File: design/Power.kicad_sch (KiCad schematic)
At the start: 77 parts

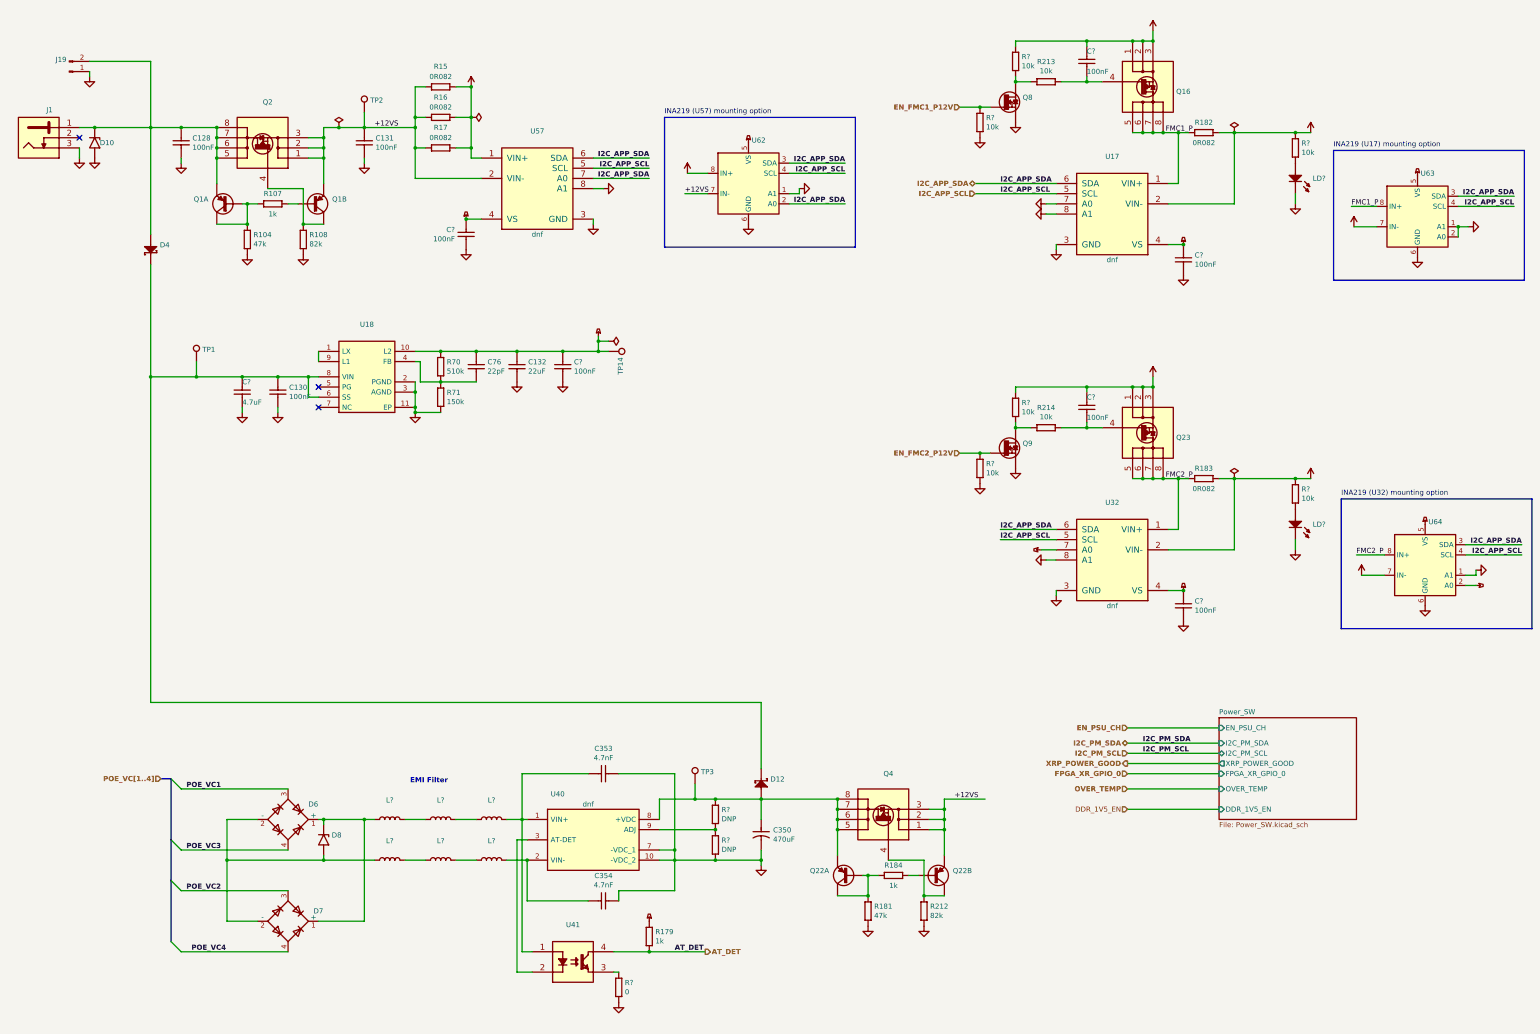
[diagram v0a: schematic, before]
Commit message: new power converter added
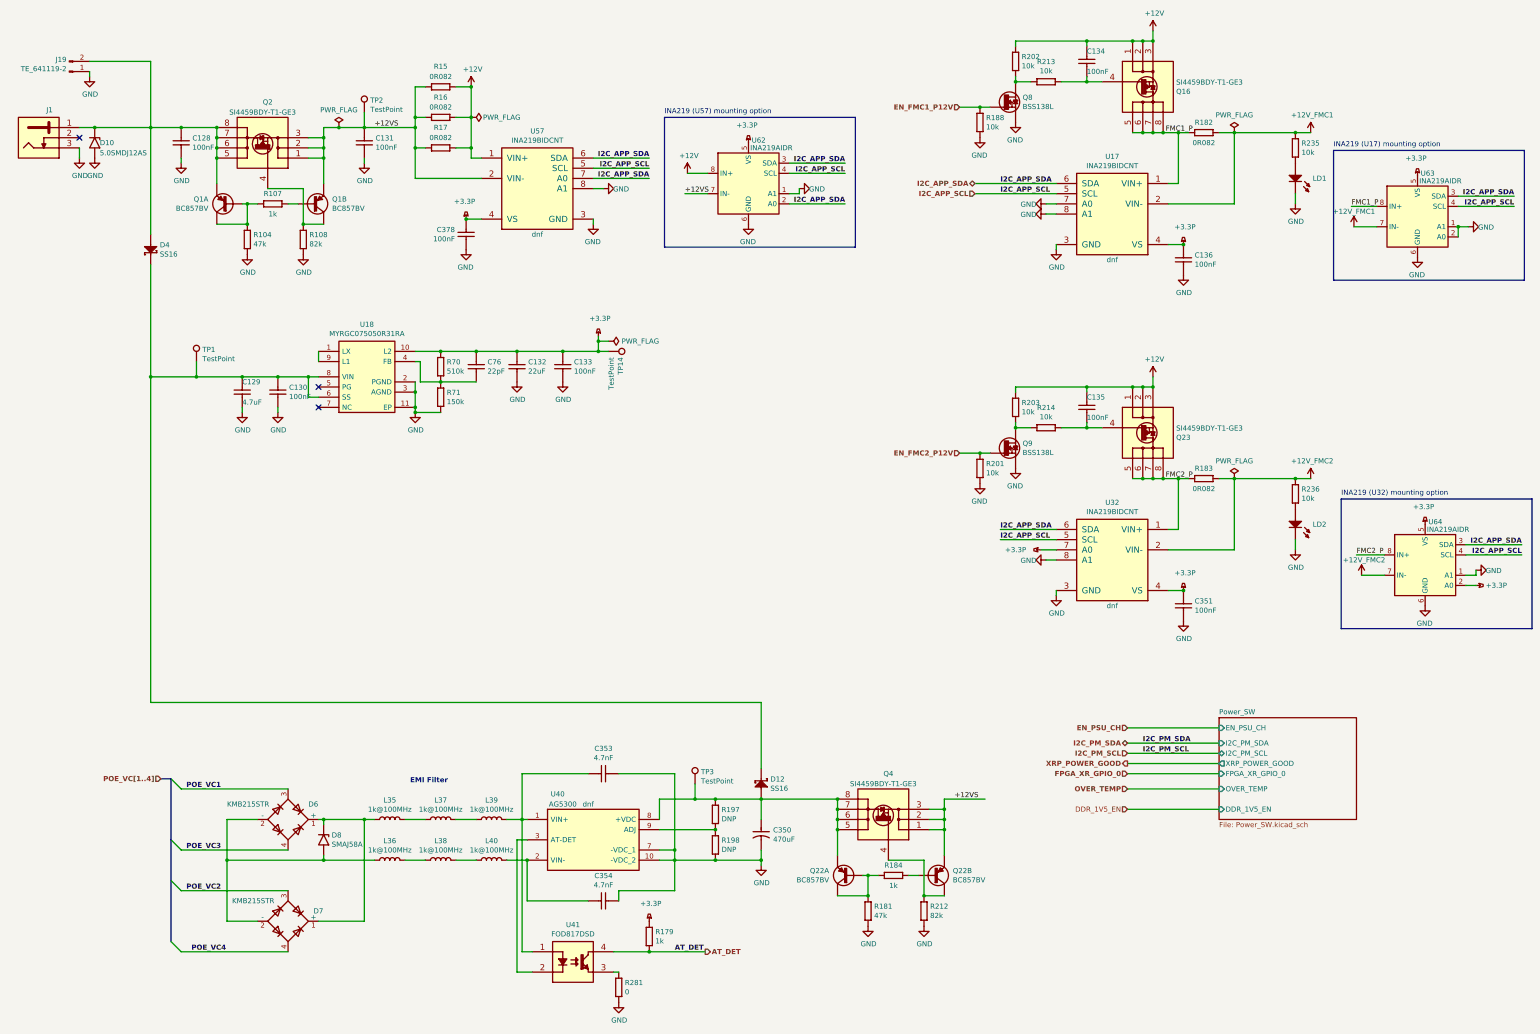
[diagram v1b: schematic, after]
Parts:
- C128, C130, C131: value (none) -> CC0402_100NF_25V_10%_X5R; footprint (none) -> Marble:CAPC1005X55N
- C129: renamed from C?; value (none) -> CC0603_4.7UF_25V_10%_X5R; footprint (none) -> Capacitors SMD:CAPC1608X90N
- C132: value (none) -> CC0603_22UF_6.3V_20%_X5R; footprint (none) -> CAPC1709X100N
- C133, C136, C351, C378: renamed from C?; value (none) -> CC0201_100NF_6.3V_10%_X5R; footprint (none) -> CAPC0603X33N
- C134, C135: renamed from C?; value (none) -> CC0402_100NF_25V_10%_X5R; footprint (none) -> Marble:CAPC1005X55N
- C350: value (none) -> CAE830-1020_470UF_16V_20%; footprint (none) -> CAPAE830X1020N
- C353, C354: value (none) -> CPER_4.7NF_400V_5%_500-250X720X650; footprint (none) -> CAPR500-250X720X650
- C76: value (none) -> CC0402_22PF_50V_5%_C0G; footprint (none) -> Capacitors SMD:CAPC1005X55N
- D10: value (none) -> 5.0SMDJ12AS; footprint (none) -> Diode_SMD:D_SMC
- D12, D4: value (none) -> SS16; footprint (none) -> DIOM5127X229N
- D6, D7: value (none) -> KMB215STR; footprint (none) -> ICs And Semiconductors SMD:SOIC254P665X290-4N
- D8: value (none) -> SMAJ58A; footprint (none) -> ICs And Semiconductors SMD:DIOM5226X262N
- J1: value (none) -> CLIFF_FC68148(DC-10A); footprint (none) -> Miscellaneous THD:CLIFF_FC68148(DC-10A)
- J19: value (none) -> TE_641119-2; footprint (none) -> Marble:641119-2
- L35, L36, L37, L38, L39, L40: renamed from L?; value (none) -> 1k@100MHz; footprint (none) -> Inductors SMD:INDC2012X145N
- LD1, LD2: renamed from LD?; value (none) -> LED_KINGBRIGHT_KPH-1608CGCK; footprint (none) -> ICs And Semiconductors SMD:LED_KINGBRIGHT_KPH-1608CGCK
- Q1, Q22: value (none) -> BC857BV; footprint (none) -> SOTFL50P160X60-6N
- Q16, Q2, Q23, Q4: value (none) -> SI4459BDY-T1-GE3; footprint (none) -> ICs And Semiconductors SMD:SOIC127P600X175-8N
- Q8, Q9: value (none) -> BSS138L; footprint (none) -> ICs And Semiconductors SMD:SOT95P240X110-3N
- R104, R181: value (none) -> R0402_47K_1%_0.0625W_100PPM; footprint (none) -> RESC1005X40N
- R107, R179, R184: value (none) -> R0402_1K_1%_0.0625W_100PPM; footprint (none) -> RESC1005X40N
- R108, R212: value (none) -> R0402_82K_1%_0.0625W_100PPM; footprint (none) -> RESC1005X40N
- R15, R16, R17, R182, R183: value (none) -> R1206_0R082_1%_0.5W_100PPM; footprint (none) -> RESC3216X80N
- R188, R201, R202, R203, R235, R236: renamed from R?; value (none) -> R0402_10K_1%_0.0625W_100PPM; footprint (none) -> RESC1005X40N
- R197, R198, R281: renamed from R?; value (none) -> R0402_0R_JUMPER; footprint (none) -> RESC1005X40N
- R213, R214: value (none) -> R0402_10K_1%_0.0625W_100PPM; footprint (none) -> RESC1005X40N
- R70: value (none) -> R0402_510K_1%_0.0625W_100PPM; footprint (none) -> Resistors SMD:RESC1005X40N
- R71: value (none) -> R0402_150K_1%_0.0625W_100PPM; footprint (none) -> Resistors SMD:RESC1005X40N
- TP1, TP14, TP2, TP3: value (none) -> TestPoint; footprint (none) -> TestPoint:TestPoint_THTPad_D1.5mm_Drill0.7mm
- U17, U32, U57: value (none) -> INA219BIDCNT; footprint (none) -> ICs And Semiconductors SMD:SOT65P280X145-8N
- U18: value (none) -> MYRGC075050R31RA; footprint (none) -> SamacSys_Parts:MYRGC075050
- U40: value (none) -> AG5300; footprint (none) -> AG5300:AG5300
- U41: value (none) -> FOD817DSD; footprint (none) -> FAIRCHILD_FOD817DSD
- U62, U63, U64: value (none) -> INA219AIDR; footprint (none) -> Package_SO:SOIC-8_3.9x4.9mm_P1.27mm

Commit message: fixed parts numners
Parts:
- C128, C130, C131, C134, C135: footprint Marble:CAPC1005X55N -> CAPC1005X55N; ALTIUM_VALUE (none) -> 100nF
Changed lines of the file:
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@@
       (effects (font (size 1.524 1.524)) (justify left) hide)
     )
-    (property "Footprint" "Marble:CAPC1005X55N" (id 2) (at 254.762 26.67 0)
+    (property "Footprint" "CAPC1005X55N" (id 2) (at 254.762 26.67 0)
       (effects (font (size 1.524 1.524)) (justify left) hide)
     )
@@
       (effects (font (size 1.524 1.524)) (justify left) hide)
     )
+    (property "ALTIUM_VALUE" "100nF" (id 40) (at 281.94 26.67 0)
+      (effects (font (size 1.27 1.27)) hide)
+    )
     (pin "1")
     (pin "2")
@@
       (effects (font (size 1.524 1.524)) (justify left) hide)
     )
-    (property "Footprint" "Marble:CAPC1005X55N" (id 2) (at 254.762 113.03 0)
+    (property "Footprint" "CAPC1005X55N" (id 2) (at 254.762 113.03 0)
       (effects (font (size 1.524 1.524)) (justify left) hide)
     )
@@
       (effects (font (size 1.524 1.524)) (justify left) hide)
     )
+    (property "ALTIUM_VALUE" "100nF" (id 40) (at 281.94 113.03 0)
+      (effects (font (size 1.27 1.27)) hide)
+    )
     (pin "1")
     (pin "2")
@@
       (effects (font (size 1.27 1.27)) (justify left) hide)
     )
-    (property "Footprint" "Marble:CAPC1005X55N" (id 2) (at 47.752 46.99 0)
+    (property "Footprint" "CAPC1005X55N" (id 2) (at 47.752 46.99 0)
       (effects (font (size 1.27 1.27)) (justify left) hide)
     )
@@
       (effects (font (size 1.27 1.27)) (justify left) hide)
     )
+    (property "ALTIUM_VALUE" "100nF" (id 39) (at 55.88 46.99 0)
+      (effects (font (size 1.27 1.27)) hide)
+    )
     (pin "1")
     (pin "2")
@@
       (effects (font (size 1.27 1.27)) (justify left) hide)
     )
-    (property "Footprint" "Marble:CAPC1005X55N" (id 2) (at 93.472 46.99 0)
+    (property "Footprint" "CAPC1005X55N" (id 2) (at 93.472 46.99 0)
       (effects (font (size 1.27 1.27)) (justify left) hide)
     )
@@
       (effects (font (size 1.27 1.27)) (justify left) hide)
     )
+    (property "ALTIUM_VALUE" "100nF" (id 39) (at 101.6 46.99 0)
+      (effects (font (size 1.27 1.27)) hide)
+    )
     (pin "1")
     (pin "2")
@@
       (effects (font (size 1.27 1.27)) (justify left) hide)
     )
-    (property "Footprint" "Marble:CAPC1005X55N" (id 2) (at 71.882 109.22 0)
+    (property "Footprint" "CAPC1005X55N" (id 2) (at 71.882 109.22 0)
       (effects (font (size 1.27 1.27)) (justify left) hide)
     )
@@
       (effects (font (size 1.27 1.27)) (justify left) hide)
     )
+    (property "ALTIUM_VALUE" "100nF" (id 39) (at 80.01 109.22 0)
+      (effects (font (size 1.27 1.27)) hide)
+    )
     (pin "1")

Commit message: LTM4673 control signals connected to MMC
LTM4673 control signals connected to MMC
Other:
- sheet Power_SW ports: added PWR_ALERT; removed none
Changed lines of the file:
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@@
     (stroke (width 0) (type default) (color 0 0 0 0))
   )
+  (wire (pts (xy 292.1 214.63) (xy 314.96 214.63))
+    (stroke (width 0) (type default) (color 0 0 0 0))
+  )
   (wire (pts (xy 304.8 147.32) (xy 304.8 134.62))
     (stroke (width 0) (type default) (color 0 0 0 0))
@@
     (effects (font (size 1.27 1.27) (thickness 0.254) bold) (justify right))
   )
+  (hierarchical_label "PWR_ALERT" (shape output) (at 292.1 214.63 180)
+    (effects (font (size 1.27 1.27) (thickness 0.254) bold) (justify right))
+  )
   (hierarchical_label "I2C_PM_SDA" (shape bidirectional) (at 292.1 200.66 180)
     (effects (font (size 1.27 1.27) (thickness 0.254) bold) (justify right))
@@
       (effects (font (size 1.27 1.27)) (justify left))
     )
+    (pin "PWR_ALERT" output (at 314.96 214.63 180)
+      (effects (font (size 1.27 1.27)) (justify left))
+    )

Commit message: connected signals to the J9 connector
connected signals to the J9 connector
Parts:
- C128, C129, C130, C131, C132, C133, C134, C135, C136, C350, C351, C353, C354, C378, C76, J1, R104, R107, R108, R15, R16, R17, R179, R181, R182, R183, R184, R188, R197, R198, R201, R202, R203, R212, R213, R214, R235, R236, R281, R70, R71: Author CERN DEM JLC -> (none)
- D10: Manufacturer Part Number (none) -> 5.0SMDJ12AS
- D12, D4, Q1, Q22, Q8, Q9, U17, U32, U41, U57: Author CERN DEM JLC -> (none); Bonding No -> (none)
- LD1, LD2: Author CERN DEM JLC -> (none); Bonding No -> (none); Color Green -> (none)
- Q16, Q2, Q23, Q4: Author CERN DEM MR -> (none); Bonding No -> (none)

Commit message: Attempt to add and improve BOM. Added new part numbers for some of the passives
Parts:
- C128, C130, C131, C134, C135, R197, R198, R281: MANUFACTURER (none) -> GENERIC
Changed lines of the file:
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@@
       (effects (font (size 1.27 1.27)) hide)
     )
+    (property "MANUFACTURER" "GENERIC" (id 41) (at 281.94 26.67 0)
+      (effects (font (size 1.27 1.27)) hide)
+    )
     (pin "1")
     (pin "2")
@@
       (effects (font (size 1.27 1.27)) hide)
     )
+    (property "MANUFACTURER" "GENERIC" (id 41) (at 281.94 113.03 0)
+      (effects (font (size 1.27 1.27)) hide)
+    )
     (pin "1")
     (pin "2")
@@
       (effects (font (size 1.524 1.524)) (justify left) hide)
     )
+    (property "MANUFACTURER" "GENERIC" (id 41) (at 165.1 257.81 0)
+      (effects (font (size 1.27 1.27)) hide)
+    )
     (pin "1")
     (pin "2")
@@
       (effects (font (size 1.27 1.27)) hide)
     )
+    (property "MANUFACTURER" "GENERIC" (id 42) (at 189.23 214.63 0)
+      (effects (font (size 1.27 1.27)) hide)
+    )
     (pin "1")
     (pin "2")
@@
       (effects (font (size 1.27 1.27)) hide)
     )
+    (property "MANUFACTURER" "GENERIC" (id 42) (at 189.23 222.25 0)
+      (effects (font (size 1.27 1.27)) hide)
+    )
     (pin "1")
     (pin "2")
@@
       (effects (font (size 1.27 1.27)) hide)
     )
+    (property "MANUFACTURER" "GENERIC" (id 40) (at 55.88 46.99 0)
+      (effects (font (size 1.27 1.27)) hide)
+    )
     (pin "1")
     (pin "2")
@@
       (effects (font (size 1.27 1.27)) hide)
     )
+    (property "MANUFACTURER" "GENERIC" (id 40) (at 101.6 46.99 0)
+      (effects (font (size 1.27 1.27)) hide)
+    )
     (pin "1")
     (pin "2")
@@
       (effects (font (size 1.27 1.27)) hide)
     )
+    (property "MANUFACTURER" "GENERIC" (id 40) (at 80.01 109.22 0)
+      (effects (font (size 1.27 1.27)) hide)
+    )

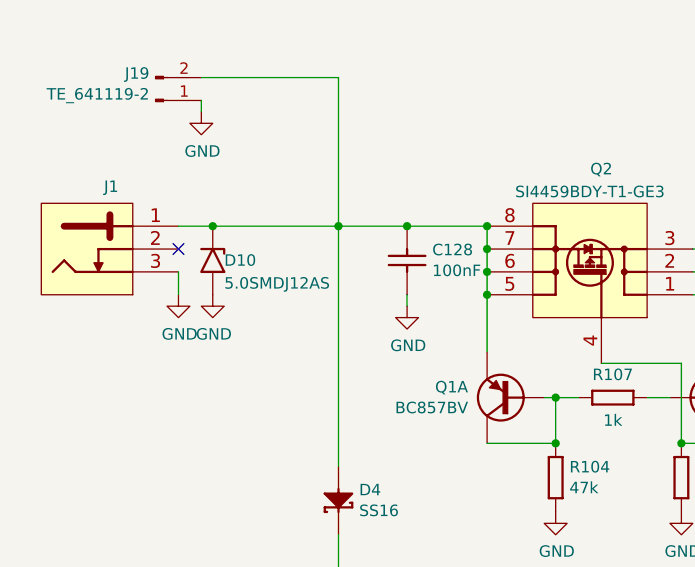
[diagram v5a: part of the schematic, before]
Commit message: Fixed part numbers for C127 and D10
Fixed part numbers for C127 and D10
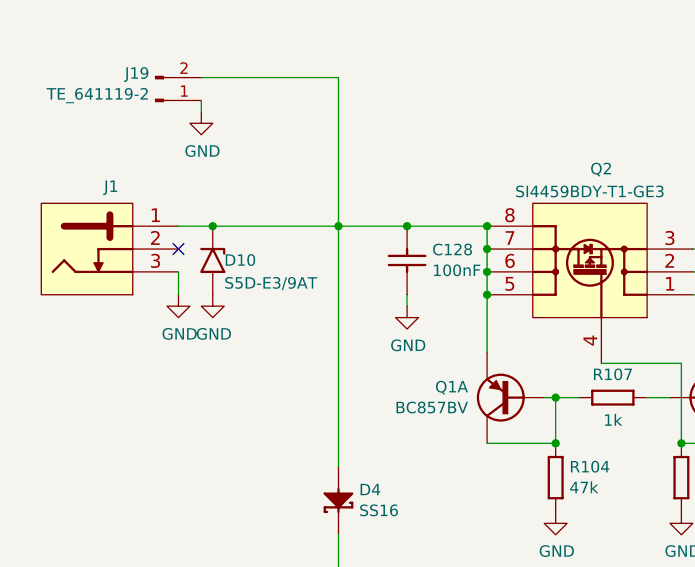
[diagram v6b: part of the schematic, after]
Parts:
- D10: value 5.0SMDJ12AS -> S5D-E3/9AT; Manufacturer Part Number 5.0SMDJ12AS -> S5D-E3/9AT; Part Number 5.0SMDJ12AS -> S5D-E3/9AT
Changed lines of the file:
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@@
       (effects (font (size 1.27 1.27)) (justify left))
     )
-    (property "Value" "5.0SMDJ12AS" (id 1) (at 35.56 53.34 90)
+    (property "Value" "S5D-E3/9AT" (id 1) (at 35.56 53.34 90)
       (effects (font (size 1.27 1.27)) (justify left))
     )
@@
       (effects (font (size 1.27 1.27)) hide)
     )
-    (property "Part Number" "5.0SMDJ12AS" (id 4) (at 34.29 50.8 90)
+    (property "Part Number" "S5D-E3/9AT" (id 4) (at 34.29 50.8 90)
       (effects (font (size 1.27 1.27)) hide)
     )
-    (property "Manufacturer Part Number" "5.0SMDJ12AS" (id 5) (at 34.29 50.8 0)
+    (property "Manufacturer Part Number" "S5D-E3/9AT" (id 5) (at 34.29 50.8 0)
       (effects (font (size 1.27 1.27)) hide)
     )

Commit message: no ERC issues
no ERC issues
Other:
- sheet Power_SW ports: added PWR_RESET; removed none
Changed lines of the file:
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@@
     (stroke (width 0) (type default) (color 0 0 0 0))
   )
-  (wire (pts (xy 292.1 217.17) (xy 314.96 217.17))
+  (wire (pts (xy 292.1 218.44) (xy 314.96 218.44))
     (stroke (width 0) (type default) (color 0 0 0 0))
   )
@@
     (stroke (width 0) (type default) (color 0 0 0 0))
   )
-  (wire (pts (xy 292.1 212.09) (xy 314.96 212.09))
+  (wire (pts (xy 292.1 210.82) (xy 314.96 210.82))
+    (stroke (width 0) (type default) (color 0 0 0 0))
+  )
+  (wire (pts (xy 292.1 213.36) (xy 314.96 213.36))
     (stroke (width 0) (type default) (color 0 0 0 0))
   )
@@
     (stroke (width 0) (type default) (color 0 0 0 0))
   )
-  (wire (pts (xy 292.1 214.63) (xy 314.96 214.63))
+  (wire (pts (xy 292.1 215.9) (xy 314.96 215.9))
     (stroke (width 0) (type default) (color 0 0 0 0))
   )
@@
     (effects (font (size 1.27 1.27) (thickness 0.254) bold) (justify right))
   )
-  (hierarchical_label "PWR_ALERT" (shape output) (at 292.1 214.63 180)
+  (hierarchical_label "PWR_ALERT" (shape output) (at 292.1 215.9 180)
     (effects (font (size 1.27 1.27) (thickness 0.254) bold) (justify right))
   )
@@
     (effects (font (size 1.27 1.27) (thickness 0.254) bold) (justify right))
   )
-  (hierarchical_label "DDR_1V5_EN" (shape input) (at 292.1 217.17 180)
+  (hierarchical_label "DDR_1V5_EN" (shape input) (at 292.1 218.44 180)
     (effects (font (size 1.27 1.27)) (justify right))
   )
@@
     (effects (font (size 1.27 1.27) (thickness 0.254) bold) (justify right))
   )
-  (hierarchical_label "OVER_TEMP" (shape input) (at 292.1 212.09 180)
+  (hierarchical_label "OVER_TEMP" (shape input) (at 292.1 213.36 180)
+    (effects (font (size 1.27 1.27) (thickness 0.254) bold) (justify right))
+  )
+  (hierarchical_label "PWR_RESET" (shape input) (at 292.1 210.82 180)
     (effects (font (size 1.27 1.27) (thickness 0.254) bold) (justify right))
   )
@@
     (pin "1")
   )
-  (sheet (at 314.96 194.31) (size 34.29 25.4) (fields_autoplaced)
+  (sheet (at 314.96 194.31) (size 34.29 26.67) (fields_autoplaced)
     (stroke (width 0) (type solid) (color 0 0 0 0))
     (fill (color 0 0 0 0.0000))
@@
       (effects (font (size 1.27 1.27)) (justify left bottom))
     )
-    (property "Sheet file" "Power_SW.kicad_sch" (id 1) (at 314.96 220.2946 0)
+    (property "Sheet file" "Power_SW.kicad_sch" (id 1) (at 314.96 221.5646 0)
       (effects (font (size 1.27 1.27)) (justify left top))
     )
@@
       (effects (font (size 1.27 1.27)) (justify left))
     )
-    (pin "OVER_TEMP" input (at 314.96 212.09 180)
+    (pin "OVER_TEMP" input (at 314.96 213.36 180)
       (effects (font (size 1.27 1.27)) (justify left))
     )
-    (pin "DDR_1V5_EN" input (at 314.96 217.17 180)
+    (pin "DDR_1V5_EN" input (at 314.96 218.44 180)
       (effects (font (size 1.27 1.27)) (justify left))
     )
@@
       (effects (font (size 1.27 1.27)) (justify left))
     )
-    (pin "PWR_ALERT" output (at 314.96 214.63 180)
+    (pin "PWR_ALERT" output (at 314.96 215.9 180)
+      (effects (font (size 1.27 1.27)) (justify left))
+    )
+    (pin "PWR_RESET" input (at 314.96 210.82 180)
       (effects (font (size 1.27 1.27)) (justify left))
     )
